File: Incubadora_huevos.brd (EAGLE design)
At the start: 100 x 80 mm, 53 parts, among them Q1 2N3904, Q2 2N3904, Q3 2N3904, T1 BT138-H, T2 BT138-H, T3 BT138-H, U1 SHT20

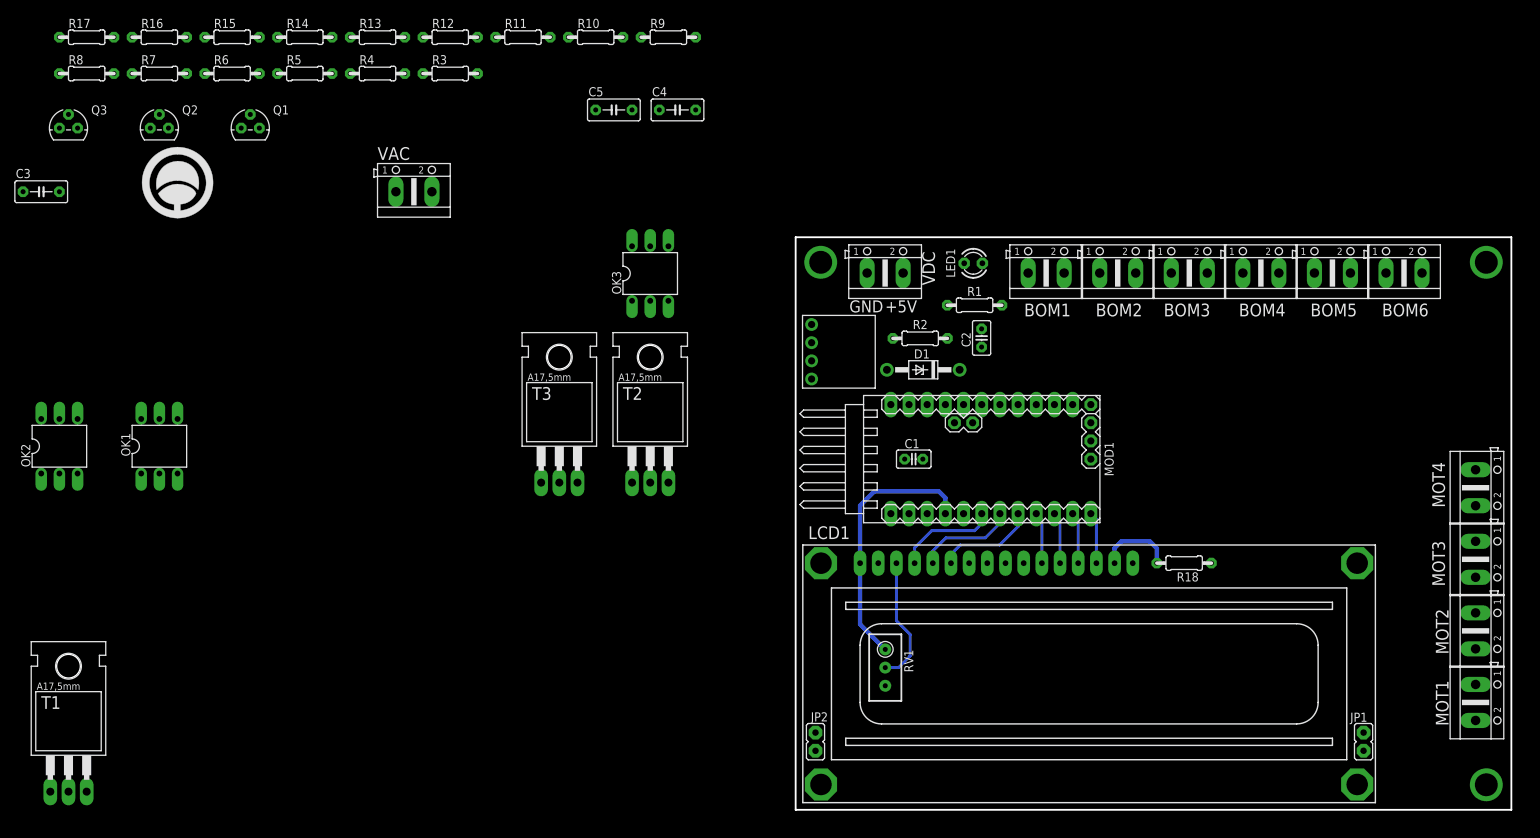
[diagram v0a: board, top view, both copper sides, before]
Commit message: Terminado ubicacion componentes. inicio ruteo
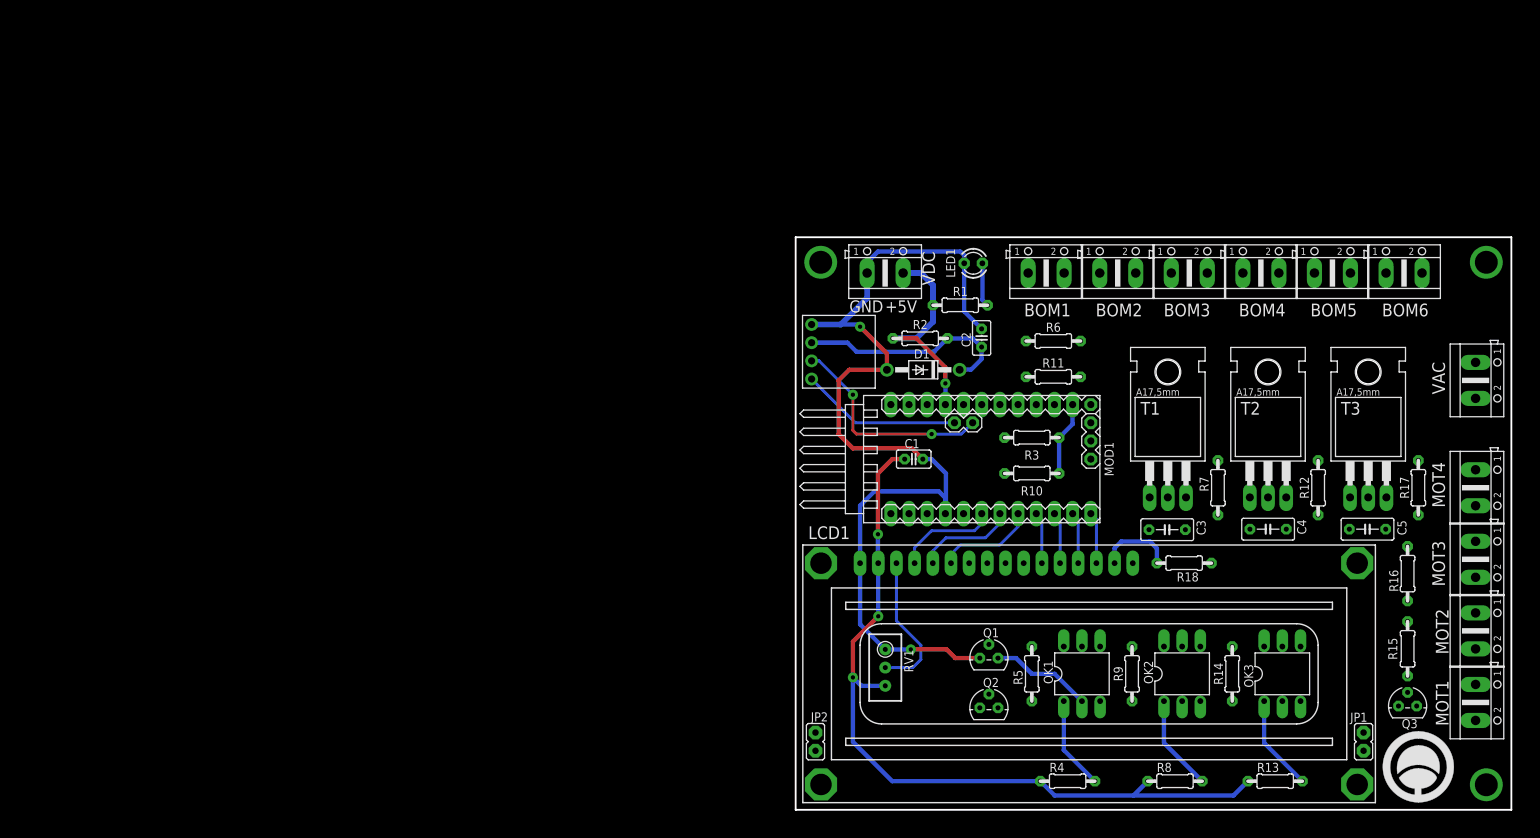
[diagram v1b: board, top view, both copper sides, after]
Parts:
- moved Q3 203.8 mm to (85.5, 14.5)
- moved R17 196.4 mm to (87.0, 45.0), turned to 90 degrees
- moved U$1 191.6 mm to (87.0, 6.00)
- moved R16 189.8 mm to (85.5, 33.0), turned to 90 degrees
- moved R15 185.1 mm to (85.5, 22.5), turned to 270 degrees
- moved R8 181.4 mm to (53.0, 4.00)
- moved C3 164.3 mm to (51.9, 39.1), turned to 180 degrees
- moved R13 162.9 mm to (67.0, 4.00)
- moved OK2 160.1 mm to (54.0, 19.0)
- moved T1 159.0 mm to (52.0, 50.0)
- moved R7 158.8 mm to (59.0, 45.0), turned to 90 degrees
- moved R14 157.2 mm to (61.0, 19.0), turned to 90 degrees
- moved VAC 150.7 mm to (95.0, 60.0), turned to 270 degrees
- moved Q2 141.4 mm to (27.0, 14.2)
- moved R4 138.1 mm to (38.0, 4.00)
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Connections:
- net LINEA: now also VAC.2; no longer VAC.1
- net NEUTR: now also VAC.1; no longer VAC.2
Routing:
- net +5V: track 0.00 -> 141.3 mm, vias 0 -> 4
- net GND: track 36.9 -> 141.7 mm, vias 0 -> 2
- net +3V3: track 0.00 -> 30.9 mm
- net SDA: track 0.00 -> 30.3 mm, vias 0 -> 2
- net SCL: track 0.00 -> 22.5 mm
- net N$6: track 0.00 -> 14.2 mm
- net N$15: track 0.00 -> 13.4 mm
- net N$8: track 0.00 -> 13.4 mm
- net N$3: track 0.00 -> 13.0 mm
- net BOM: track 0.00 -> 10.4 mm
- net N$1: track 0.00 -> 6.16 mm
- net N$34: track 17.9 -> 20.3 mm

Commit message: Terminado BRD, listo para fabricar
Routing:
- net NEUTR: track 0.00 -> 175.1 mm, vias 0 -> 3
- net LOAD2: track 0.00 -> 128.3 mm, vias 0 -> 1
- net LINEA: track 0.00 -> 122.8 mm
- net GND: track 141.7 -> 251.9 mm, vias 2 -> 3
- net MOT: track 0.00 -> 80.3 mm, vias 0 -> 1
- net N$11: track 0.00 -> 78.9 mm, vias 0 -> 2
- net LOAD1: track 0.00 -> 75.4 mm
- net +5V: track 141.3 -> 214.3 mm, vias 4 -> 6
- net LOAD3: track 0.00 -> 72.8 mm
- net N$7: track 0.00 -> 72.3 mm
- net N$2: track 0.00 -> 70.5 mm, vias 0 -> 2
- net N$5: track 0.00 -> 64.5 mm, vias 0 -> 3
- net N$12: track 0.00 -> 31.0 mm, vias 0 -> 1
- net N$14: track 0.00 -> 30.8 mm, vias 0 -> 1
- net N$18: track 0.00 -> 24.3 mm
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- added copper zone on layer 1, net GND
- added copper zone on layer 16, net GND
- added copper zone on layer 1, net T1
- added copper zone on layer 16, net T1
- added copper zone on layer 1, net T2
- added copper zone on layer 16, net T2
- added copper zone on layer 1, net T3
- added copper zone on layer 16, net T3
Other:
- board text added: "LINEA"
- board text added: "NEUTRO"

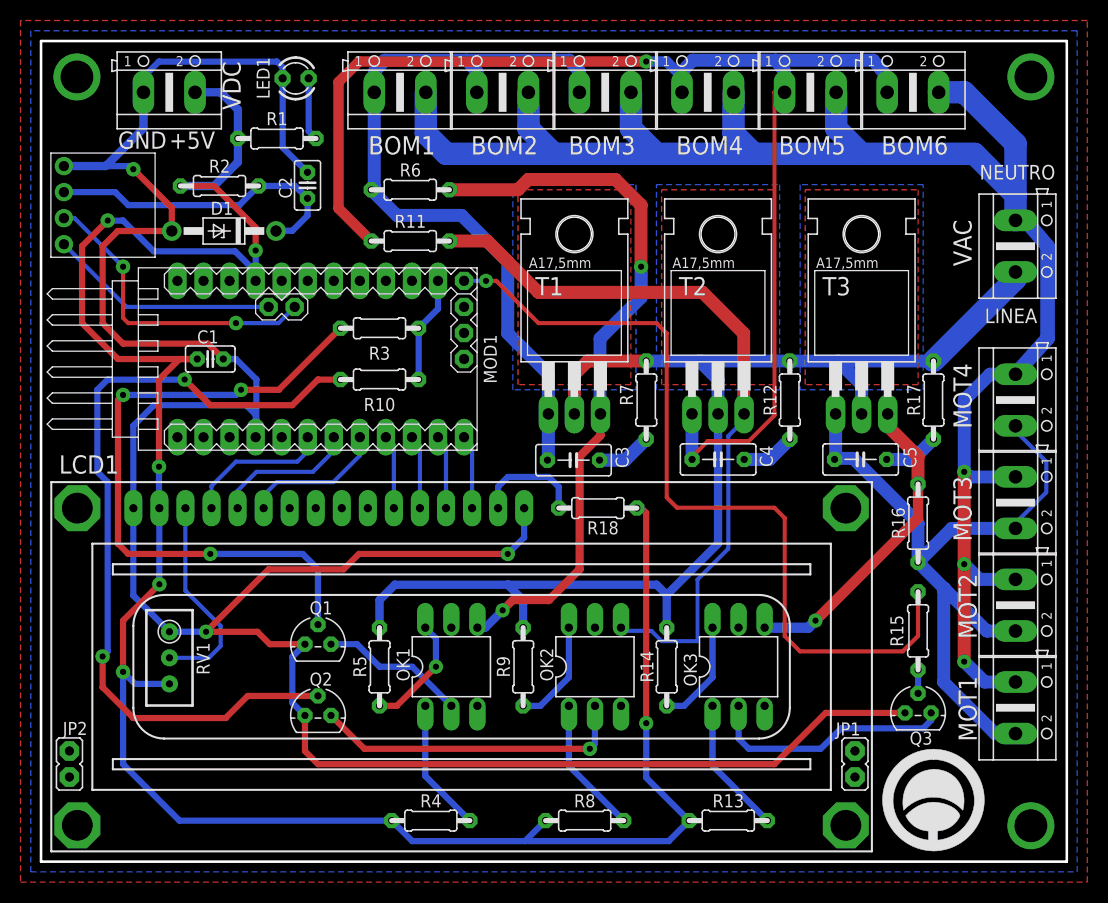
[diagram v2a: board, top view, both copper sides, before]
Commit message: Se modifico la etapa de potencia ya que la anterior se calentaba mucho
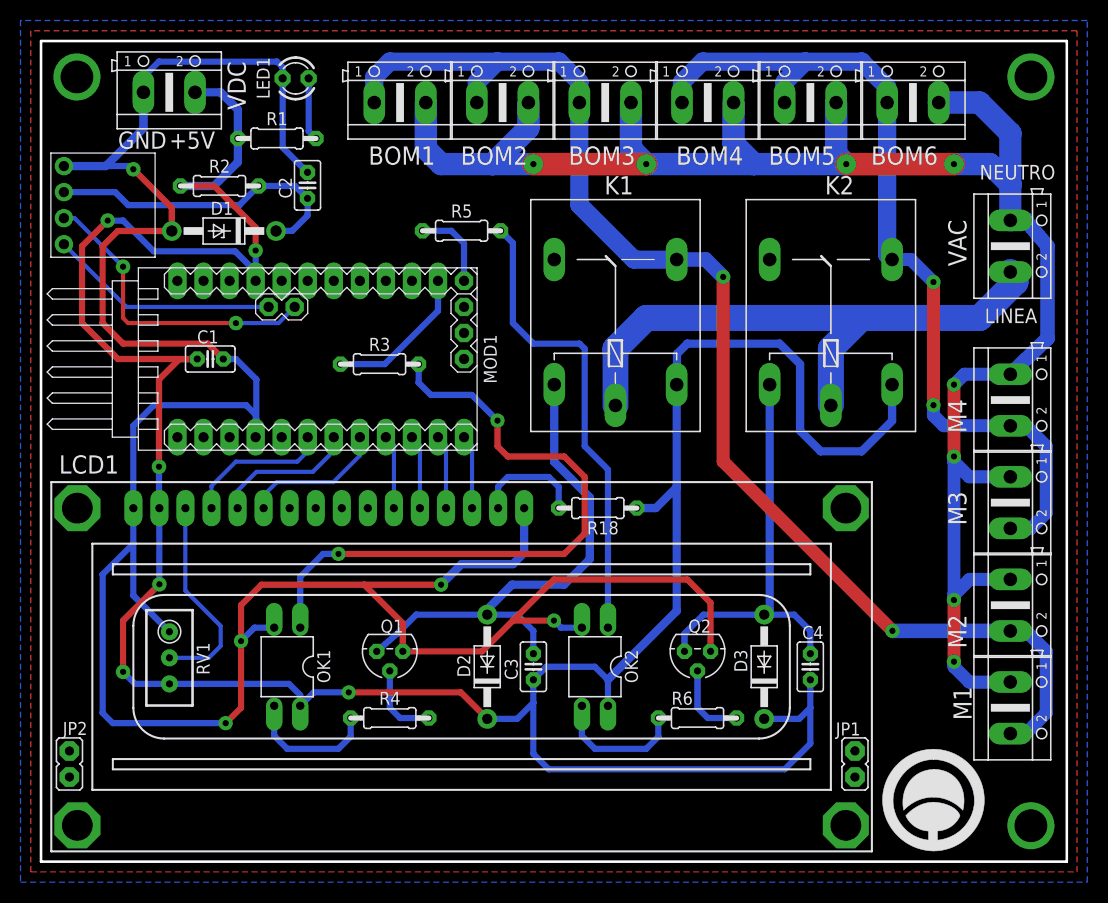
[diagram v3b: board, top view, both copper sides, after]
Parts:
- removed C5: 10n, rcl:C050-030X075
- removed MOT1, MOT2, MOT3, MOT4: (no value), con-ptr500:AK500/2
- removed OK3: MOC3021M, optocoupler:DIL06
- removed Q3: 2N3904, transistor-small-signal:TO92D
- removed R10, R15: 5k1, rcl:0204/7
- removed R11, R14, R16, R9: 330R, rcl:0204/7
- removed R12, R17, R7: 39R, rcl:0204/7
- removed R13, R8: 220R, rcl:0204/7
- removed T1, T2, T3: BT138-H, triac:TO220BH
- added D2, D3: 1N4004, adafruit:DO41-10
- added K1, K2: G5L, relay:G5LE
- added M1, M2, M3, M4: (no value), con-ptr500:AK500/2
- C3, C4: value 10n -> 100n; device rcl:C050-030X075 -> rcl:C025-025X050
- OK1, OK2: value MOC3021M -> PC817; device optocoupler:DIL06 -> optocoupler:DIL04
- R3: value 5k1 -> 10k
- R4: value 220R -> 1k
- R5: value 330R -> 10k
- R6: value 330R -> 1k
- moved R6 58.6 mm to (64.0, 14.0)
- moved R5 43.2 mm to (41.0, 61.5), turned to 0 degrees
- moved Q2 37.5 mm to (64.0, 20.5), turned to 180 degrees
- moved C4 22.1 mm to (75.0, 19.0), turned to 90 degrees
- moved C3 20.5 mm to (48.0, 19.0), turned to 90 degrees
- moved OK1 16.0 mm to (24.0, 19.0), turned to 180 degrees
- moved R4 10.8 mm to (34.0, 14.0)
- moved Q1 7.03 mm to (34.0, 20.5), turned to 180 degrees
- moved R3 3.50 mm to (33.0, 48.5), turned to 0 degrees
- moved BOM1 1.00 mm to (35.0, 74.0)
- moved BOM2 1.00 mm to (45.0, 74.0)
- moved BOM3 1.00 mm to (55.0, 74.0)
- moved BOM4 1.00 mm to (65.0, 74.0)
- moved BOM5 1.00 mm to (75.0, 74.0)
- moved BOM6 1.00 mm to (85.0, 74.0)
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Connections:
- removed net LOAD3: C5.2, MOT1.2, MOT2.2, MOT3.2, MOT4.2, R16.1, T3.T1
- removed net N$10: OK2.6, R9.1
- removed net N$11: Q2.B, R10.2
- removed net N$12: OK2.2, Q2.C
- removed net N$13: C4.1, R12.1
- removed net N$14: OK3.4, R16.2, T3.G
- removed net N$15: OK3.1, R13.2
- removed net N$16: OK3.6, R14.1
- removed net N$17: Q3.B, R15.2
- removed net N$18: OK3.2, Q3.C
- removed net N$19: C5.1, R17.1
- removed net N$9: C3.1, R7.1
- new net N$21: C3.2, D2.A, K1.2, Q1.C
- net +5V: now also C3.1, C4.1, D2.C, D3.C, K1.1, K2.1, OK1.4, OK2.4; no longer R13.1, R4.1, R8.1
- net BOM: no longer R10.1
- net GND: now also OK1.2, OK2.2; no longer Q3.E
- net LINEA: now also K1.P, K2.P; no longer R12.2, R14.2, R17.2, R5.2, R7.2, R9.2, T1.T2, T2.T2, T3.T2
- net LOAD1: now also K1.S, M1.2, M2.2; no longer C3.2, R6.1, T1.T1
- net LOAD2: now also K2.S, M3.2, M4.2; no longer C4.2, R11.1, T2.T1
- net MOT: now also R5.1; no longer R15.1
- net N$2: now also OK1.3, R4.1; no longer OK1.4, R6.2, T1.G
- net N$3: now also Q1.B; no longer OK1.1
- net N$4: now also OK1.1, R3.2; no longer OK1.6, R5.1
- net N$5: now also C4.2, D3.A, K2.2, Q2.C; no longer Q1.B, R3.2
- net N$6: now also OK2.3, R6.1; no longer OK1.2, Q1.C
- net N$7: now also Q2.B, R6.2; no longer OK2.4, R11.2, T2.G
- net N$8: now also R5.2; no longer R8.2
- net NEUTR: now also M1.1, M2.1, M3.1, M4.1; no longer MOT1.1, MOT2.1, MOT3.1, MOT4.1
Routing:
- net N$11: track 78.9 -> 0.00 mm, vias 2 -> 0
- net LOAD3: track 72.8 -> 0.00 mm
- net MOT: track 80.3 -> 8.20 mm, vias 1 -> 0
- net +5V: track 214.3 -> 281.8 mm
- net LINEA: track 122.8 -> 58.1 mm
- net N$7: track 72.3 -> 7.82 mm
- net N$2: track 70.5 -> 13.2 mm, vias 2 -> 0
- net N$4: track 11.3 -> 63.2 mm, vias 1 -> 2
- net N$21: track 0.00 -> 50.8 mm
- net LOAD1: track 75.4 -> 125.2 mm, vias 0 -> 2
- net LOAD2: track 128.3 -> 87.5 mm, vias 1 -> 2
- net N$8: track 13.4 -> 45.7 mm
- net N$12: track 31.0 -> 0.00 mm, vias 1 -> 0
- net N$14: track 30.8 -> 0.00 mm, vias 1 -> 0
- net N$18: track 24.3 -> 0.00 mm
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- removed copper zone on layer 1, net T1
- removed copper zone on layer 16, net T1
- removed copper zone on layer 1, net T2
- removed copper zone on layer 16, net T2
- removed copper zone on layer 1, net T3
- removed copper zone on layer 16, net T3
